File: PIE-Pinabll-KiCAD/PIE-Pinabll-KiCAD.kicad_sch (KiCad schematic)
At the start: 3 parts, among them U1 SC0915, U2 Adafruit MAX98357A Breakout, U3 Adafruit microSD 3V Breakout

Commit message: Inital design for electrical systems
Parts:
- added J1: Flipper Left, 1935161:PHOENIX_1935161, symbol carter_terminal_blocks:Terminal_01x02
- added J2: Flipper Right, 1935161:PHOENIX_1935161, symbol carter_terminal_blocks:Terminal_01x02
- added J3: Slingshot Right, 1935161:PHOENIX_1935161, symbol carter_terminal_blocks:Terminal_01x02
- added J4: Slingshot Left, 1935161:PHOENIX_1935161, symbol carter_terminal_blocks:Terminal_01x02
- added J5: Flipper Button Left, 1935161:PHOENIX_1935161, symbol carter_terminal_blocks:Terminal_01x02
- added J6: Flipper Button Right, 1935161:PHOENIX_1935161, symbol carter_terminal_blocks:Terminal_01x02
- added J7, J8: Dropdown1, 1935161:PHOENIX_1 1935174, symbol carter_terminal_blocks:Terminal_01x03
- added Q1, Q2, Q3, Q4: VNP20N07-E, TO-220_STM, symbol carter_kicad_symbols:VNP20N07-E
- added R1, R3, R5, R7: 10k, symbol Device:R
- added R10, R11, R13, R15: 5k, symbol Device:R
- added R12, R14, R16, R9: R_Photo, symbol Device:R_Photo
- added R2, R4, R6, R8: 110, symbol Device:R
- added U4: MCP3008, MCU-MCP3008-I_P_DIP16-7.62MM_:DIP16-2.54-19.2X7.62MM, symbol carter_kicad_symbols:MCP3008 Analog to Digital Converter (ADC)
- added U5: MCP23017, carter_kicad_footprints:DIP787, symbol carter_kicad_symbols:MCP23017 I/O Expander
- added U6: TLC5947_Adafruit, symbol carter_kicad_symbols:Adafruit TLC5947 LED
- added U7: LLS, symbol carter_kicad_symbols:Logic Level Shifter Adafruit
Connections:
- net GND: now also U1.13 (GND), U1.18 (GND), U1.23 (GND), U1.28 (GND), U1.3 (GND), U1.38 (GND), U1.8 (GND), U1.D2 (GND), U2.2 (GND), J5.2, J6.2, J7.3, J8.3, Q1.3, Q2.3, Q3.3, Q4.3, R1.1, R12.2, R14.2, R16.2, R3.1, R5.1, R7.1, R9.2, U4.14 (AGND), U4.9 (DGND), U5.10 (VSS), U5.15 (A0), U5.16 (A1), U5.17 (A2), U6.5 (GND), U7.12 (GND), U7.6 (GND)
- net VCC: now also U1.36 (3V3_OUT), U2.1 (VIN), R10.1, R11.1, R13.1, R15.1, U4.15 (VREF), U4.16 (VDD), U5.18 (~{RESET}), U5.9 (VDD), U6.6 (V+), U7.1 (LV)
- net FL_O: now reaches U1.1 (GP0)
- net FL_O: now also R1.2, R2.2
- net LDR_ADC_MOSI: now reaches U1.10 (GP7)
- net LDR_ADC_MOSI: now also U4.11 (DIN)
- net LDR_ADC_MISO: now reaches U1.11 (GP8)
- net LDR_ADC_MISO: now also U4.12 (DOUT)
- net LDR_ADC_CS: now reaches U1.12 (GP9)
- net LDR_ADC_CS: now also U4.10 (SHDN/~{CS})
- net SDU_IO_SDA: now reaches U1.14 (GP10)
- net SDU_IO_SDA: now also U5.13 (SDA)
- net SDU_IO_SCL: now reaches U1.15 (GP11)
- net SDU_IO_SCL: now also U5.12 (SCL)
- net LED_LAT: now reaches U1.16 (GP12)
- net LED_LAT: now also U6.1 (LAT)
- net SDU_IO_CLK: now reaches U1.17 (GP13)
- net LED_CLK: now reaches U1.19 (GP14)
- net LED_CLK: now also U6.3 (CLK)
- net FR_O: now reaches U1.2 (GP1)
- net FR_O: now also R3.2, R4.2
- net LED_MOSI: now reaches U1.20 (GP15)
- net LED_MOSI: now also U6.4 (DIN)
- net AMP_LRC: now reaches U1.21 (GP16)
- net AMP_LRC: now also U2.7 (LRC)
- net AMP_BLCK: now reaches U1.22 (GP17)
- net AMP_DIN: now reaches U1.29 (GP22)
- net AMP_DIN: now also U2.5 (DIN)
- net DD1_PWM: now reaches U1.31 (GP26)
- net DD1_PWM: now also U7.2 (A1)
- net DD2_PWM: now reaches U1.32 (GP27)
- net DD2_PWM: now also U7.3 (A2)
- net SL_O: now reaches U1.4 (GP2)
- net SL_O: now also R7.2, R8.2
- net +5V: now reaches U1.40 (VBUS)
- net +5V: now also J7.1, J8.1, U7.7 (HV)
- net SR_O: now reaches U1.5 (GP3)
- net SR_O: now also R5.2, R6.2
- net FBL_O: now reaches U1.6 (GP4)
- net FBL_O: now also J5.1
- net FBR_O: now reaches U1.7 (GP5)
- net FBR_O: now also J6.1
- net LDR_ADC_CLK: now reaches U1.9 (GP6)
- net LDR_ADC_CLK: now also U4.13 (CLK)
- net AMP_BCLK: now reaches U2.6 (BCLK)
- new net: J1.2, Q1.2
- new net: J7.2, U7.8 (B1)
- new net: J8.2, U7.9 (B2)
- new net: Q2.1, R4.1
- new net: J2.2, Q2.2
- new net: J3.2, Q3.2
- new net: J4.2, Q4.2
- new net: Q4.1, R8.1
- new net: Q3.1, R6.1
- new net: Q1.1, R2.1
- new net +12V: J1.1, J2.1, J3.1, J4.1
- new net LDR_ADC_CH0: R10.2, R9.1, U4.1 (CH0)
- new net LDR_ADC_CH1: R11.2, R12.1, U4.2 (CH1)
- new net LDR_ADC_CH2: R13.2, R14.1, U4.3 (CH2)
- new net LDR_ADC_CH3: R15.2, R16.1, U4.4 (CH3)
- new net LDR_ADC_CH4: U4.5 (CH4)
- new net LDR_ADC_CH5: U4.6 (CH5)
- new net LDR_ADC_CH6: U4.7 (CH6)
- new net LDR_ADC_CH7: U4.8 (CH7)
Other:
- note added: "24-channels each connected to LED anode"
- note added: "Each channel connected to rollover V divider"
- note added: "Each pin connected to one side of standup switch NOTE: configure pull-up Rs in code"
- note added: "I2C Address: 0x20"
- note added: "I2S"
- note added: "Loch Ness First Rollover"
- note added: "Loch Ness Second Rollover"
- note added: "Rear Left Rollover"
- note added: "Rear Right Rollover"
- note added: "SPI"
- company: (none) -> Olin Pinball PIE Team
- title: (none) -> Pinball Machine Electrical Systems
- moved on the sheet: U1, U2, U3

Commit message: Add scoring LCD; various minor updates
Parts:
- added U8: MCP23017, carter_kicad_footprints:DIP787, symbol carter_kicad_symbols:MCP23017 I/O Expander
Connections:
- net GND: now also U8.16 (A1), U8.17 (A2)
- net SDU_IO_SCL: now also U8.12 (SCL)
- net SDU_IO_SDA: now also U8.13 (SDA)
- net VCC: now also U8.15 (A0), U8.18 (~{RESET}), U8.9 (VDD)
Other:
- note added: "Connected to LCD I/O"
- note added: "Each pin connected toone side of standup switch NOTE: configure pull-up Rs in code"
- note added: "I2C Address: 0x21"
- note added: "Set Internal Pullup"
- note removed: "Each pin connected to one side of standup switch NOTE: configure pull-up Rs in code"
- moved on the sheet: U1, U4, U5, U6

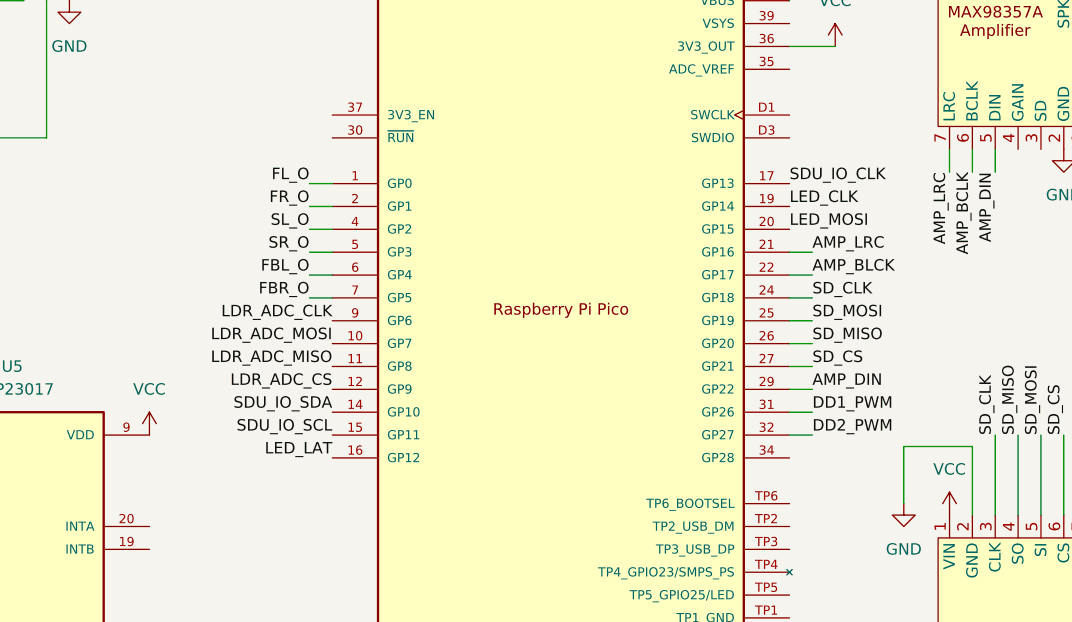
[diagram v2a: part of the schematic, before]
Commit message: Update schematic to use correct SPI pinouts
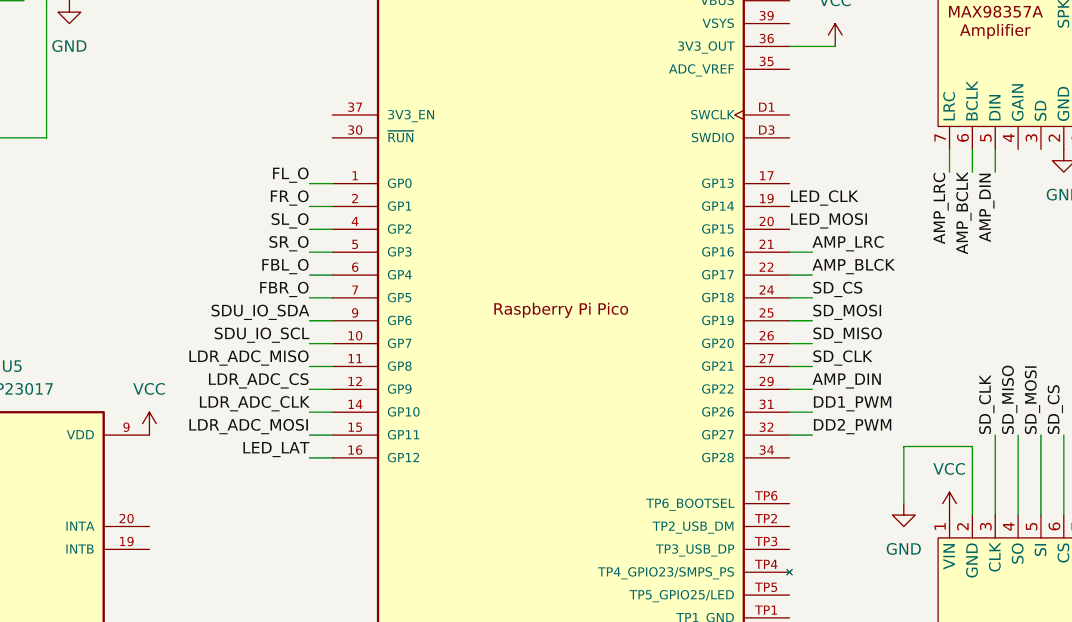
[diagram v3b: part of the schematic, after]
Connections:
- net LDR_ADC_CLK: now also U1.14 (GP10); no longer U1.9 (GP6)
- net LDR_ADC_MOSI: now also U1.15 (GP11); no longer U1.10 (GP7)
- net SDU_IO_SCL: now also U1.10 (GP7); no longer U1.15 (GP11)
- net SDU_IO_SDA: now also U1.9 (GP6); no longer U1.14 (GP10)
- net SD_CLK: now also U1.27 (GP21); no longer U1.24 (GP18)
- net SD_CS: now also U1.24 (GP18); no longer U1.27 (GP21)
- net SDU_IO_CLK: no longer names the net of U1.17 (GP13)
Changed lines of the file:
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@@
     (stroke (width 0) (type default))
   )
+  (wire (pts (xy 185.42 69.85) (xy 187.96 69.85))
+    (stroke (width 0) (type default))
+  )
   (wire (pts (xy 68.58 99.06) (xy 68.58 96.52))
     (stroke (width 0) (type default))
@@
     (stroke (width 0) (type default))
   )
+  (wire (pts (xy 185.42 59.69) (xy 187.96 59.69))
+    (stroke (width 0) (type default))
+  )
   (wire (pts (xy 251.46 78.74) (xy 259.08 78.74))
     (stroke (width 0) (type default))
@@
     (stroke (width 0) (type default))
   )
-  (wire (pts (xy 185.42 62.23) (xy 187.96 62.23))
+  (wire (pts (xy 185.42 54.61) (xy 187.96 54.61))
     (stroke (width 0) (type default))
   )
-  (wire (pts (xy 185.42 54.61) (xy 187.96 54.61))
+  (wire (pts (xy 185.42 62.23) (xy 187.96 62.23))
     (stroke (width 0) (type default))
   )
@@
     (stroke (width 0) (type default))
   )
-  (wire (pts (xy 241.3 69.85) (xy 238.76 69.85))
-    (stroke (width 0) (type default))
-  )
   (wire (pts (xy 175.26 147.32) (xy 175.26 152.4))
     (stroke (width 0) (type default))
@@
     (stroke (width 0) (type default))
   )
-  (wire (pts (xy 185.42 59.69) (xy 187.96 59.69))
+  (wire (pts (xy 241.3 57.15) (xy 238.76 57.15))
     (stroke (width 0) (type default))
   )
-  (wire (pts (xy 241.3 62.23) (xy 238.76 62.23))
+  (wire (pts (xy 55.88 101.6) (xy 55.88 96.52))
     (stroke (width 0) (type default))
   )
-  (wire (pts (xy 241.3 57.15) (xy 238.76 57.15))
+  (wire (pts (xy 241.3 62.23) (xy 238.76 62.23))
     (stroke (width 0) (type default))
   )
-  (wire (pts (xy 55.88 101.6) (xy 55.88 96.52))
+  (wire (pts (xy 241.3 69.85) (xy 238.76 69.85))
     (stroke (width 0) (type default))
   )
@@
     (stroke (width 0) (type default))
   )
+  (wire (pts (xy 241.3 67.31) (xy 238.76 67.31))
+    (stroke (width 0) (type default))
+  )
   (wire (pts (xy 22.86 152.4) (xy 22.86 151.13))
     (stroke (width 0) (type default))
   )
+  (wire (pts (xy 185.42 77.47) (xy 187.96 77.47))
+    (stroke (width 0) (type default))
+  )
   (wire (pts (xy 127 97.79) (xy 127 95.25))
     (stroke (width 0) (type default))
@@
     (stroke (width 0) (type default))
   )
-  (wire (pts (xy 241.3 64.77) (xy 238.76 64.77))
+  (wire (pts (xy 22.86 161.29) (xy 22.86 162.56))
     (stroke (width 0) (type default))
   )
-  (wire (pts (xy 22.86 161.29) (xy 22.86 162.56))
+  (wire (pts (xy 185.42 64.77) (xy 187.96 64.77))
     (stroke (width 0) (type default))
   )
@@
     (stroke (width 0) (type default))
   )
-  (wire (pts (xy 271.78 45.72) (xy 275.59 45.72))
+  (wire (pts (xy 185.42 74.93) (xy 187.96 74.93))
     (stroke (width 0) (type default))
   )
-  (wire (pts (xy 241.3 67.31) (xy 238.76 67.31))
+  (wire (pts (xy 271.78 45.72) (xy 275.59 45.72))
     (stroke (width 0) (type default))
   )
@@
     (stroke (width 0) (type default))
   )
+  (wire (pts (xy 185.42 80.01) (xy 187.96 80.01))
+    (stroke (width 0) (type default))
+  )
   (wire (pts (xy 21.59 33.02) (xy 25.4 33.02))
     (stroke (width 0) (type default))
@@
     (stroke (width 0) (type default))
   )
+  (wire (pts (xy 185.42 72.39) (xy 187.96 72.39))
+    (stroke (width 0) (type default))
+  )
   (wire (pts (xy 185.42 52.07) (xy 187.96 52.07))
     (stroke (width 0) (type default))
@@
     (stroke (width 0) (type default))
   )
+  (wire (pts (xy 241.3 64.77) (xy 238.76 64.77))
+    (stroke (width 0) (type default))
+  )
   (wire (pts (xy 261.62 48.26) (xy 261.62 45.72))
     (stroke (width 0) (type default))
@@
     (stroke (width 0) (type default))
   )
+  (wire (pts (xy 185.42 67.31) (xy 187.96 67.31))
+    (stroke (width 0) (type default))
+  )
   (wire (pts (xy 33.02 52.07) (xy 34.29 52.07))
     (stroke (width 0) (type default))
@@
     (effects (font (size 1.27 1.27)) (justify right bottom))
   )
-  (label "SDU_IO_SDA" (at 187.96 74.93 180) (fields_autoplaced)
+  (label "SDU_IO_SDA" (at 185.42 64.77 180) (fields_autoplaced)
     (effects (font (size 1.27 1.27)) (justify right bottom))
   )
@@
     (effects (font (size 1.27 1.27)) (justify left bottom))
   )
-  (label "LDR_ADC_MOSI" (at 187.96 67.31 180) (fields_autoplaced)
+  (label "LDR_ADC_MOSI" (at 185.42 77.47 180) (fields_autoplaced)
     (effects (font (size 1.27 1.27)) (justify right bottom))
   )
@@
     (effects (font (size 1.27 1.27)) (justify left bottom))
   )
-  (label "LDR_ADC_CS" (at 187.96 72.39 180) (fields_autoplaced)
+  (label "LDR_ADC_CS" (at 185.42 72.39 180) (fields_autoplaced)
     (effects (font (size 1.27 1.27)) (justify right bottom))
   )
@@
     (effects (font (size 1.27 1.27)) (justify left bottom))
   )
-  (label "LDR_ADC_MISO" (at 187.96 69.85 180) (fields_autoplaced)
+  (label "LDR_ADC_MISO" (at 185.42 69.85 180) (fields_autoplaced)
     (effects (font (size 1.27 1.27)) (justify right bottom))
   )
@@
     (effects (font (size 1.27 1.27)) (justify right bottom))
   )
-  (label "SDU_IO_SCL" (at 187.96 77.47 180) (fields_autoplaced)
+  (label "SDU_IO_SCL" (at 185.42 67.31 180) (fields_autoplaced)
     (effects (font (size 1.27 1.27)) (justify right bottom))
   )
@@
     (effects (font (size 1.27 1.27)) (justify right bottom))
   )
-  (label "SD_CLK" (at 241.3 62.23 0) (fields_autoplaced)
+  (label "SD_CLK" (at 241.3 69.85 0) (fields_autoplaced)
     (effects (font (size 1.27 1.27)) (justify left bottom))
   )
-  (label "LDR_ADC_CLK" (at 187.96 64.77 180) (fields_autoplaced)
+  (label "LDR_ADC_CLK" (at 185.42 74.93 180) (fields_autoplaced)
     (effects (font (size 1.27 1.27)) (justify right bottom))
   )
@@
     (effects (font (size 1.27 1.27)) (justify left bottom))
   )
-  (label "SD_CS" (at 241.3 69.85 0) (fields_autoplaced)
+  (label "SD_CS" (at 241.3 62.23 0) (fields_autoplaced)
     (effects (font (size 1.27 1.27)) (justify left bottom))
   )
@@
     (effects (font (size 1.27 1.27)) (justify left bottom))
   )
-  (label "LED_LAT" (at 187.96 80.01 180) (fields_autoplaced)
+  (label "LED_LAT" (at 185.42 80.01 180) (fields_autoplaced)
     (effects (font (size 1.27 1.27)) (justify right bottom))
   )
@@
     (effects (font (size 1.27 1.27)) (justify left bottom))
   )
-  (label "SDU_IO_CLK" (at 238.76 49.53 0) (fields_autoplaced)
-    (effects (font (size 1.27 1.27)) (justify left bottom))
-  )

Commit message: Update schematic to relfect on-board wiring
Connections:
- net SD_MOSI is gone; now on net LED_MOSI: U1.25 (GP19), U3.5 (SI)
- net AMP_BLCK: now also U1.32 (GP27); no longer U1.22 (GP17)
- net AMP_DIN: now also U1.31 (GP26); no longer U1.29 (GP22)
- net AMP_LRC: now also U1.34 (GP28); no longer U1.21 (GP16)
- net DD1_PWM: now also U1.19 (GP14); no longer U1.31 (GP26)
- net DD2_PWM: now also U1.20 (GP15); no longer U1.32 (GP27)
- net LED_CLK: now also U1.24 (GP18), U3.3 (CLK); no longer U1.19 (GP14)
- net LED_LAT: now also U1.29 (GP22); no longer U1.16 (GP12)
- net LED_MOSI: no longer U1.20 (GP15)
- net SD_CS: now also U1.22 (GP17); no longer U1.24 (GP18)
- net SD_CLK: no longer names the net of U1.27 (GP21)
- net SD_CLK: no longer U3.3 (CLK)
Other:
- moved on the sheet: U2, U3
